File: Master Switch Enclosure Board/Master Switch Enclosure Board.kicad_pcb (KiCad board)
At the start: 2 copper layers, 40 parts, among them IC1 LM5155DSSR, J1 Harness In A, J2 Harness In B, J3 Harness Out, J4 Screw_Terminal_01x04, J5 Screw_Terminal_01x04, J6 20-pin MicroFit, J7 4-pin MicroFit, Q1 CSD18537NQ5A

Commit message: finished routing
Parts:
- removed G***: LOGO, Global Libraries:rylan
- J3: footprint Connector_Molex:Molex_Micro-Fit_3.0_43045-2012_2x10_P3.00mm_Vertical -> Connector_Molex:Molex_Micro-Fit_3.0_43045-2412_2x12_P3.00mm_Vertical
- moved D1 104.2 mm to (102.3, 78.0), turned to 0 degrees
- moved L1 100.3 mm to (105.3, 98.8), turned to -90 degrees
- moved C11 99.9 mm to (104.0, 90.3), turned to 0 degrees
- moved C12 88.3 mm to (110.4, 78.0), turned to -90 degrees
- moved J2 87.5 mm to (115.5, 144.0)
- moved J1 87.5 mm to (80.2, 144.0)
- moved C6 86.1 mm to (114.6, 103.9), turned to 90 degrees
- moved C3 83.5 mm to (114.6, 100.5), turned to 90 degrees
- moved Q1 83.1 mm to (112.2, 86.9), turned to 0 degrees
- moved R8 82.8 mm to (113.3, 77.2), turned to -90 degrees
- moved R9 81.6 mm to (113.3, 80.6), turned to -90 degrees
- moved R2 80.6 mm to (117.6, 103.9), turned to 90 degrees
- moved R1 77.9 mm to (117.6, 100.5), turned to 90 degrees
- moved C4 73.3 mm to (121.4, 103.2), turned to 90 degrees
- moved R6 72.2 mm to (117.8, 89.0), turned to 90 degrees
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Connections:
- J1 pad 1: LVBAT_in -> LV_mastersw_out
- J1 pad 10: LV_mastersw_out -> LVBAT_in
- J1 pad 12: SHDN2_in -> CANL_VCU2
- J1 pad 13: SHDN2_out -> CANH_VCU2
- J1 pad 14: RST_out -> CANL_ret_Tel
- J1 pad 15: BYP_out -> CANH_ret_Tel
- J1 pad 16: CHRG_in -> BYP_out
- J1 pad 17: TSALSafe_pt -> CANL_Tel
- J1 pad 18: TSALEnergized_pt -> CANH_Tel
- J1 pad 19: CANH_EM -> TSALEnergized_pt
- J1 pad 2: LVBAT_in -> LV_mastersw_out
- J1 pad 20: CANL_EM -> TSALSafe_pt
- J1 pad 3: LVBAT_in -> LV_mastersw_out
- J1 pad 4: LVBAT_in -> LV_mastersw_out
- J1 pad 5: LVBAT_in -> LV_mastersw_out
- J1 pad 6: LV_mastersw_out -> LVBAT_in
- J1 pad 7: LV_mastersw_out -> LVBAT_in
- J1 pad 8: LV_mastersw_out -> LVBAT_in
- J1 pad 9: LV_mastersw_out -> LVBAT_in
- J2 pad 1: CANH_Tel -> GND
- J2 pad 10: CANL_VCU3 -> CHRG_in
- J2 pad 11: CANH_VCU4 -> CANL_ret_VCU3
- J2 pad 12: CANL_VCU4 -> CANH_ret_VCU3
- J2 pad 13: CANH_ret_VCU2 -> CANL_VCU4
- J2 pad 14: CANL_ret_VCU2 -> CANH_VCU4
- J2 pad 15: CANH_ret_VCU3 -> RST_out
- J2 pad 16: CANL_ret_VCU3 -> VCUWake_out
- J2 pad 17: GND -> CANL_VCU1
- J2 pad 18: BSPDTest_in -> CANH_VCU1
- J2 pad 19: BSPDTest_out -> SHDN2_in
- J2 pad 2: CANL_Tel -> CANL_ret_VCU2
- J2 pad 20: VCUWake_out -> SHDN2_out
- J2 pad 3: CANH_ret_Tel -> CANH_ret_VCU2
- J2 pad 4: CANL_ret_Tel -> CANL_VCU3
- J2 pad 5: CANH_VCU1 -> CANH_VCU3
- J2 pad 6: CANL_VCU1 -> BSPDTest_out
- J2 pad 7: CANH_VCU2 -> BSPDTest_in
- J2 pad 8: CANL_VCU2 -> CANL_EM
- J2 pad 9: CANH_VCU3 -> CANH_EM
- J3 pad 1: LV_mastersw_out -> GND
- J3 pad 10: CANH_VCU2 -> CANL_VCU1
- J3 pad 11: CANL_VCU2 -> CANH_VCU2
- J3 pad 12: CANH_VCU3 -> CANL_VCU2
- J3 pad 13: CANL_VCU3 -> CANH_VCU3
- J3 pad 14: CANH_VCU4 -> CANL_VCU3
- J3 pad 15: CANL_VCU4 -> CANH_VCU4
- J3 pad 16: CANH_ret_VCU2 -> CANL_VCU4
- J3 pad 17: CANL_ret_VCU2 -> CANH_ret_VCU2
- J3 pad 18: CANH_ret_VCU3 -> CANL_ret_VCU2
- J3 pad 19: CANL_ret_VCU3 -> CANH_ret_VCU3
- J3 pad 20: GND -> CANL_ret_VCU3
- J3 pad 6: TSALSafe_pt -> LV_mastersw_out
- J3 pad 7: TSALEnergized_pt -> TSALSafe_pt
- J3 pad 8: CANH_VCU1 -> TSALEnergized_pt
- J3 pad 9: CANL_VCU1 -> CANH_VCU1
- J4 pad 2: BYP_out -> LVBAT_sw
- J5 pad 4: LVBAT_sw -> BYP_out
- J6 pad 10: SEPIC_out -> RST_out
- J6 pad 11: VCUWake_out -> CHRG_in
- J6 pad 14: CANL_VCU1 -> CANH_VCU1
- J6 pad 15: CANH_VCU1 -> CANL_VCU1
- J6 pad 7: SEPIC_out -> VCUWake_out
- J6 pad 8: RST_out -> SEPIC_out
- J6 pad 9: CHRG_in -> SEPIC_out
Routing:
- net CHRG_in: track 0.00 -> 193.2 mm
- net CANH_VCU1: track 0.00 -> 188.1 mm, vias 0 -> 1
- net SHDN2_out: track 0.00 -> 185.1 mm
- net CANH_EM: track 0.00 -> 184.9 mm
- net CANL_VCU1: track 0.00 -> 183.3 mm, vias 0 -> 1
- net CANL_EM: track 0.00 -> 182.4 mm
- net SHDN2_in: track 0.00 -> 180.7 mm
- net BSPDTest_in: track 0.00 -> 169.5 mm, vias 0 -> 1
- net BSPDTest_out: track 0.00 -> 168.6 mm, vias 0 -> 1
- net VCUWake_out: track 0.00 -> 163.2 mm
- net RST_out: track 0.00 -> 146.1 mm, vias 0 -> 1
- net CANH_VCU3: track 0.00 -> 121.0 mm
- net CANL_VCU3: track 0.00 -> 116.2 mm
- net CANH_VCU4: track 0.00 -> 106.2 mm
- net CANL_VCU4: track 0.00 -> 100.5 mm
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- added copper zone on B.Cu, net BYP_out
- added copper zone on F.Cu, net BYP_out
- added copper zone on B.Cu, net LVBAT_in
- added copper zone on F.Cu, net LVBAT_sw
- added copper zone on B.Cu, net LV_mastersw_out
- added copper zone on F.Cu, net LV_mastersw_out
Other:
- board outline added: 120 x 117 mm
- board text added: "DPDT IN 1A"
- board text added: "DPDT OUT 1"
- board text added: "DPDT OUT 2"
- board text added: "GND"
- board text added: "LV SW IN"
- board text added: "LV SW OUT"

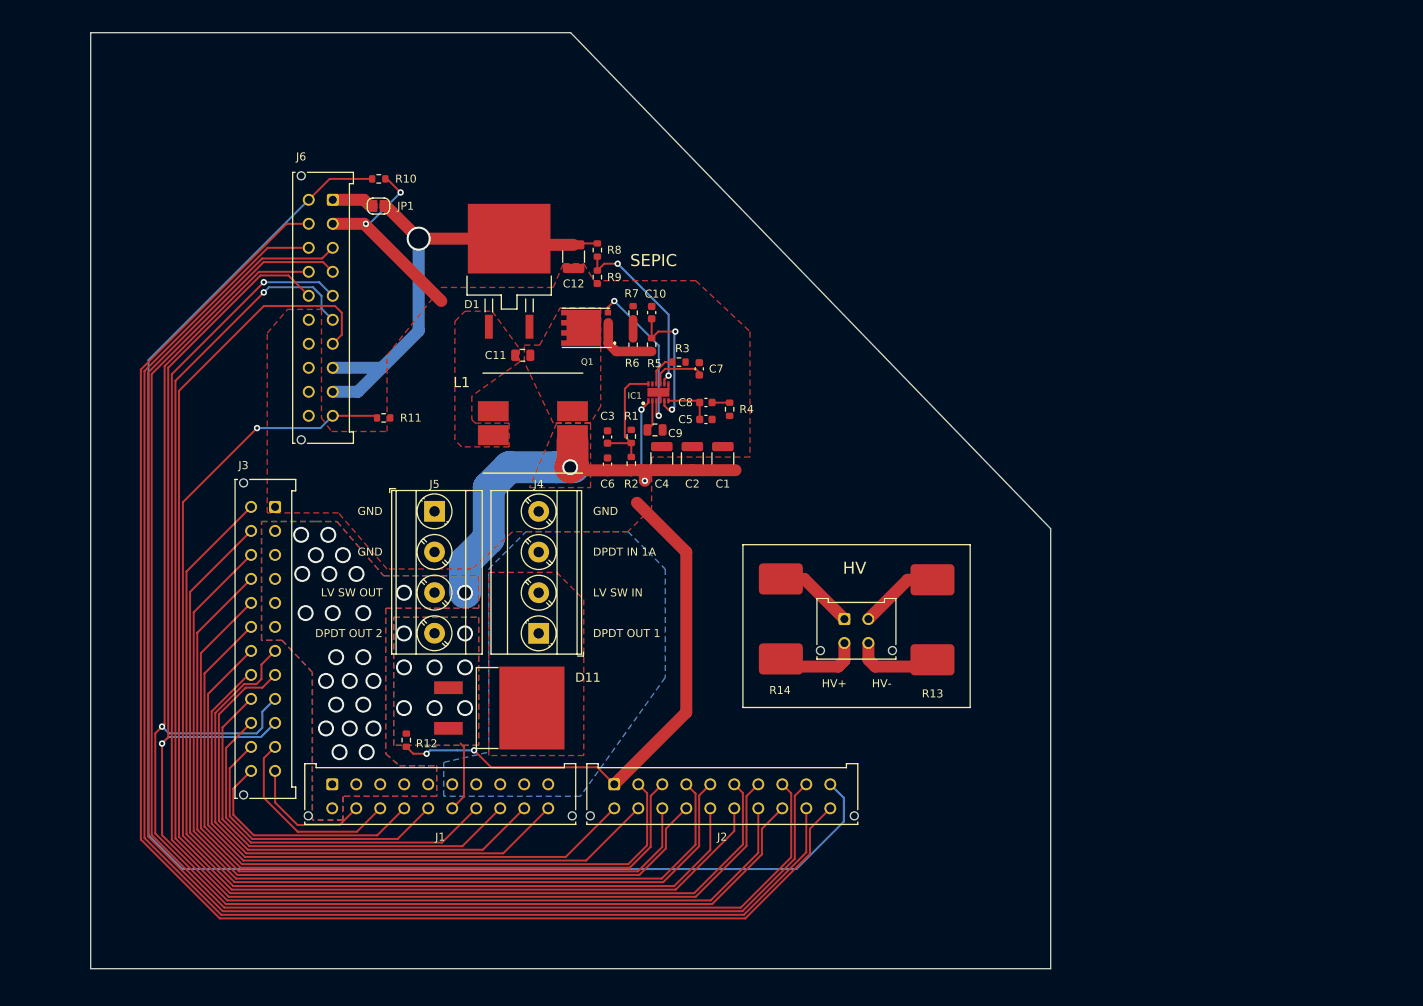
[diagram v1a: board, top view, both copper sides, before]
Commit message: less resistance, more spacing
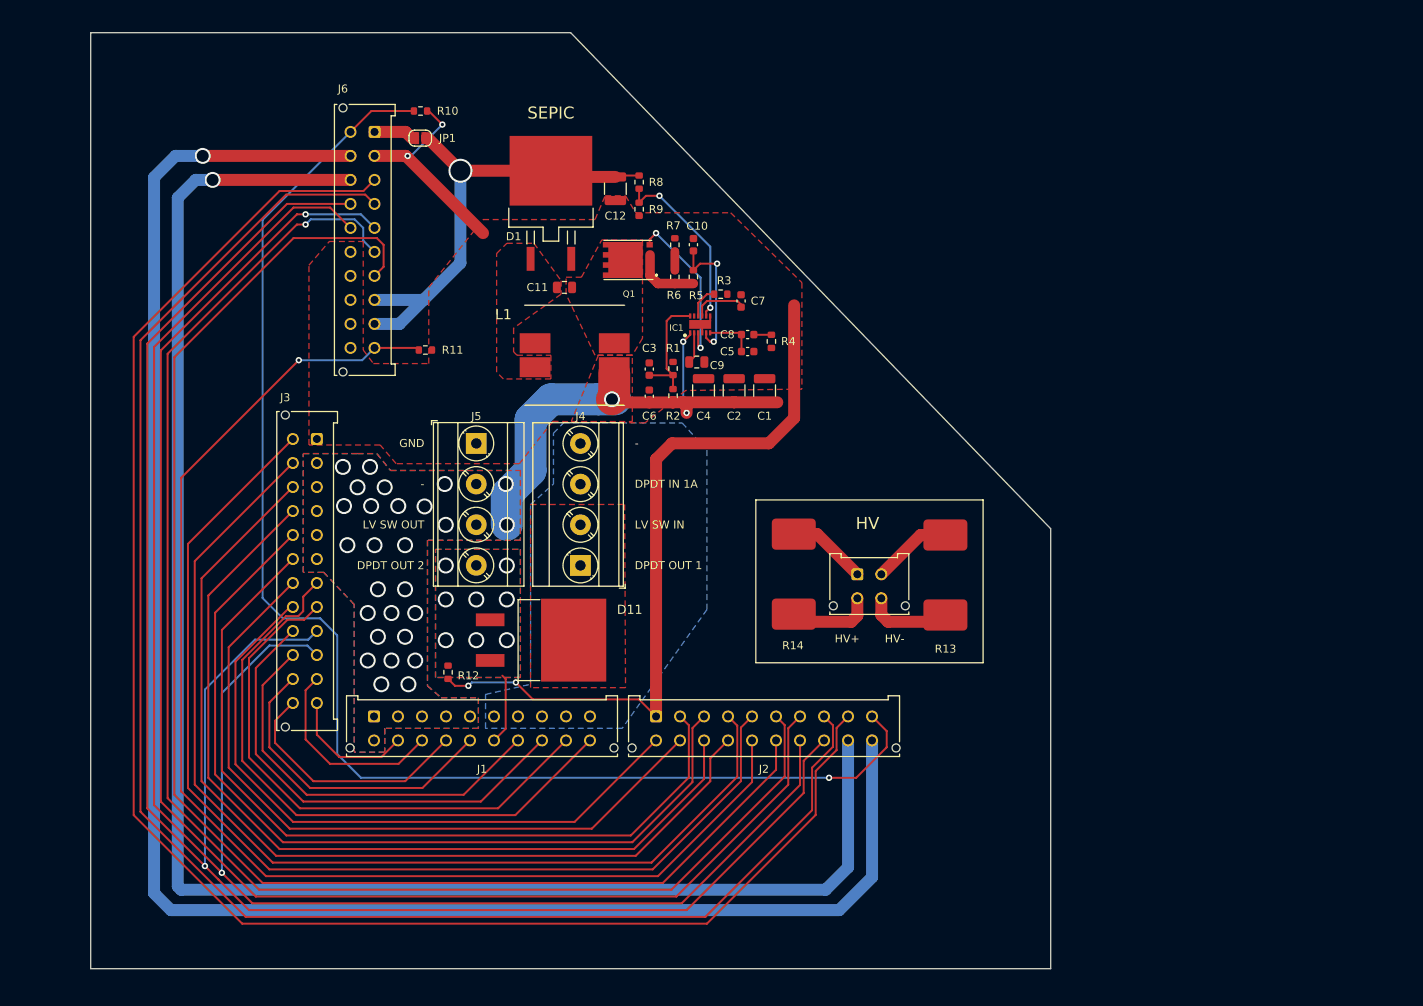
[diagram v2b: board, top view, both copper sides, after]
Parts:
- moved C1 9.96 mm to (134.2, 94.7)
- moved C10 9.96 mm to (125.3, 76.5)
- moved C2 9.96 mm to (130.4, 94.7)
- moved C3 9.96 mm to (119.8, 92.0)
- moved C5 9.96 mm to (132.1, 89.9)
- moved C6 9.96 mm to (119.8, 95.4)
- moved C8 9.96 mm to (132.1, 87.7)
- moved IC1 9.96 mm to (126.2, 86.5)
- moved J1 9.96 mm to (85.4, 135.5)
- moved J2 9.96 mm to (120.7, 135.5)
- moved L1 9.96 mm to (110.5, 90.3)
- moved Q1 9.96 mm to (117.4, 78.4)
- moved R1 9.96 mm to (122.8, 92.0)
- moved R2 9.96 mm to (122.8, 95.4)
- moved R3 9.96 mm to (128.8, 82.7)
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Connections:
- J4 pad 4: GND -> LVBAT_in
- J5 pad 2: GND -> LV_mastersw_out
- Q1 pad 9: (no net) -> Net-(C11-Pad2)
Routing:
- net CANH_VCU1: track 188.1 -> 230.8 mm
- net CANL_VCU1: track 183.3 -> 224.9 mm
- net SHDN2_out: track 185.1 -> 224.6 mm, vias 0 -> 1
- net SHDN2_in: track 180.7 -> 209.6 mm, vias 0 -> 1
- net GND: track 103.1 -> 127.2 mm
- net CANH_EM: track 184.9 -> 208.5 mm
- net CANL_EM: track 182.4 -> 204.4 mm
- net BSPDTest_in: track 169.5 -> 189.1 mm
- net CHRG_in: track 193.2 -> 174.0 mm, vias 0 -> 1
- net BSPDTest_out: track 168.6 -> 186.7 mm
- net VCUWake_out: track 163.2 -> 181.0 mm
- net RST_out: track 146.1 -> 161.6 mm
- net CANH_VCU3: track 121.0 -> 135.6 mm
- net CANL_VCU3: track 116.2 -> 129.6 mm
- net CANH_VCU4: track 106.2 -> 118.8 mm
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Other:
- board text added: "-"

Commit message: done
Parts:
- added G***: LOGO, Global Libraries:rylan, F.Cu at (146.0, 99.4)
- added M1: MountingHole_3.2mm_M3_Pad, MountingHole:MountingHole_3.2mm_M3_Pad, F.Cu at (55.0, 55.0)
- added M2: MountingHole_3.2mm_M3_Pad, MountingHole:MountingHole_3.2mm_M3_Pad, F.Cu at (107.0, 55.0)
- added M3: MountingHole_3.2mm_M3_Pad, MountingHole:MountingHole_3.2mm_M3_Pad, F.Cu at (165.0, 115.0)
- added M4: MountingHole_3.2mm_M3_Pad, MountingHole:MountingHole_3.2mm_M3_Pad, F.Cu at (165.0, 162.0)
- added M5: MountingHole_3.2mm_M3_Pad, MountingHole:MountingHole_3.2mm_M3_Pad, F.Cu at (55.0, 162.0)
- moved J7 5.66 mm to (140.3, 118.7)
- moved R13 5.66 mm to (148.3, 118.8)
- moved R14 5.66 mm to (129.3, 118.7)
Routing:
- net SEPIC_out: track 60.0 -> 11.4 mm, vias 1 -> 0
- net GND: track 127.2 -> 100.4 mm, vias 4 -> 9
- net SHDN2_in: track 209.6 -> 212.8 mm, vias 1 -> 0
- net CANL_ret_VCU3: track 82.6 -> 83.6 mm
- net CHRG_in: track 174.0 -> 173.3 mm, vias 1 -> 0
- net TSALSafe_pt: track 77.1 -> 77.7 mm
- net Net-(C10-Pad2): track 17.4 -> 18.0 mm
- net SHDN2_out: track 224.6 -> 224.4 mm, vias 1 -> 0
- added copper zone on B.Cu, net GND
- added copper zone on F.Cu, net SEPIC_out

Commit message: bom
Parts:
- removed C4: 10u, Capacitor_SMD:C_1210_3225Metric
- added C13: 4.7u, Capacitor_SMD:C_0805_2012Metric_Pad1.18x1.45mm_HandSolder, F.Cu at (109.0, 82.7)
- added C14: 22u, Capacitor_SMD:C_1206_3216Metric_Pad1.33x1.80mm_HandSolder, F.Cu at (117.4, 69.8)
- added C15: 22u, Capacitor_SMD:C_1206_3216Metric_Pad1.33x1.80mm_HandSolder, F.Cu at (119.9, 69.8)
- C1, C2: value 10u -> 22u; footprint Capacitor_SMD:C_1210_3225Metric -> Capacitor_SMD:C_1206_3216Metric_Pad1.33x1.80mm_HandSolder
- C10, C3, C5, C6, C7, C8: footprint Capacitor_SMD:C_0603_1608Metric -> Capacitor_SMD:C_0603_1608Metric_Pad1.08x0.95mm_HandSolder
- C11: value 9.4u -> 4.7u; footprint Capacitor_SMD:C_0805_2012Metric -> Capacitor_SMD:C_0805_2012Metric_Pad1.18x1.45mm_HandSolder
- C12: value 66u -> 22u; footprint Capacitor_SMD:C_1210_3225Metric -> Capacitor_SMD:C_1206_3216Metric_Pad1.33x1.80mm_HandSolder
- C9: footprint Capacitor_SMD:C_0805_2012Metric -> Capacitor_SMD:C_0805_2012Metric_Pad1.18x1.45mm_HandSolder
- R1, R10, R11, R12, R2, R3, R4, R5, R6, R7, R8, R9: footprint Resistor_SMD:R_0603_1608Metric -> Resistor_SMD:R_0603_1608Metric_Pad0.98x0.95mm_HandSolder
- moved C1 6.38 mm to (128.0, 96.2), turned to 0 degrees
- moved R8 4.41 mm to (123.0, 68.7)
- moved R9 4.41 mm to (123.0, 72.1)
- moved C2 3.49 mm to (133.6, 96.2), turned to 0 degrees
- moved C11 1.30 mm to (109.0, 80.6)
- moved D1 0.85 mm to (107.5, 68.7)
- moved C12 0.68 mm to (115.0, 69.8)
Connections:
- C1 pad 2: GND -> Net-(C1-Pad2)
- C2 pad 1: LV_mastersw_out -> Net-(C1-Pad2)
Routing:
- net SEPIC_out: track 11.4 -> 0.00 mm
- net LV_mastersw_out: track 63.6 -> 53.9 mm
- net Net-(C1-Pad2): track 0.00 -> 2.39 mm
- net /SEPIC/FB: track 22.6 -> 20.4 mm
- net GND: vias 9 -> 12
